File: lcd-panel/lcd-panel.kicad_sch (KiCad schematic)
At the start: 30 parts, among them J1 USB wire, J2 LCD FPC connector, J3 Fan Socket, Q1 AO3400A, U1 FT232HL-REEL, U2 93LC56BT-I/OT, U3 USBLC6-2SC6, Y1 12 MHz, 20 pF load

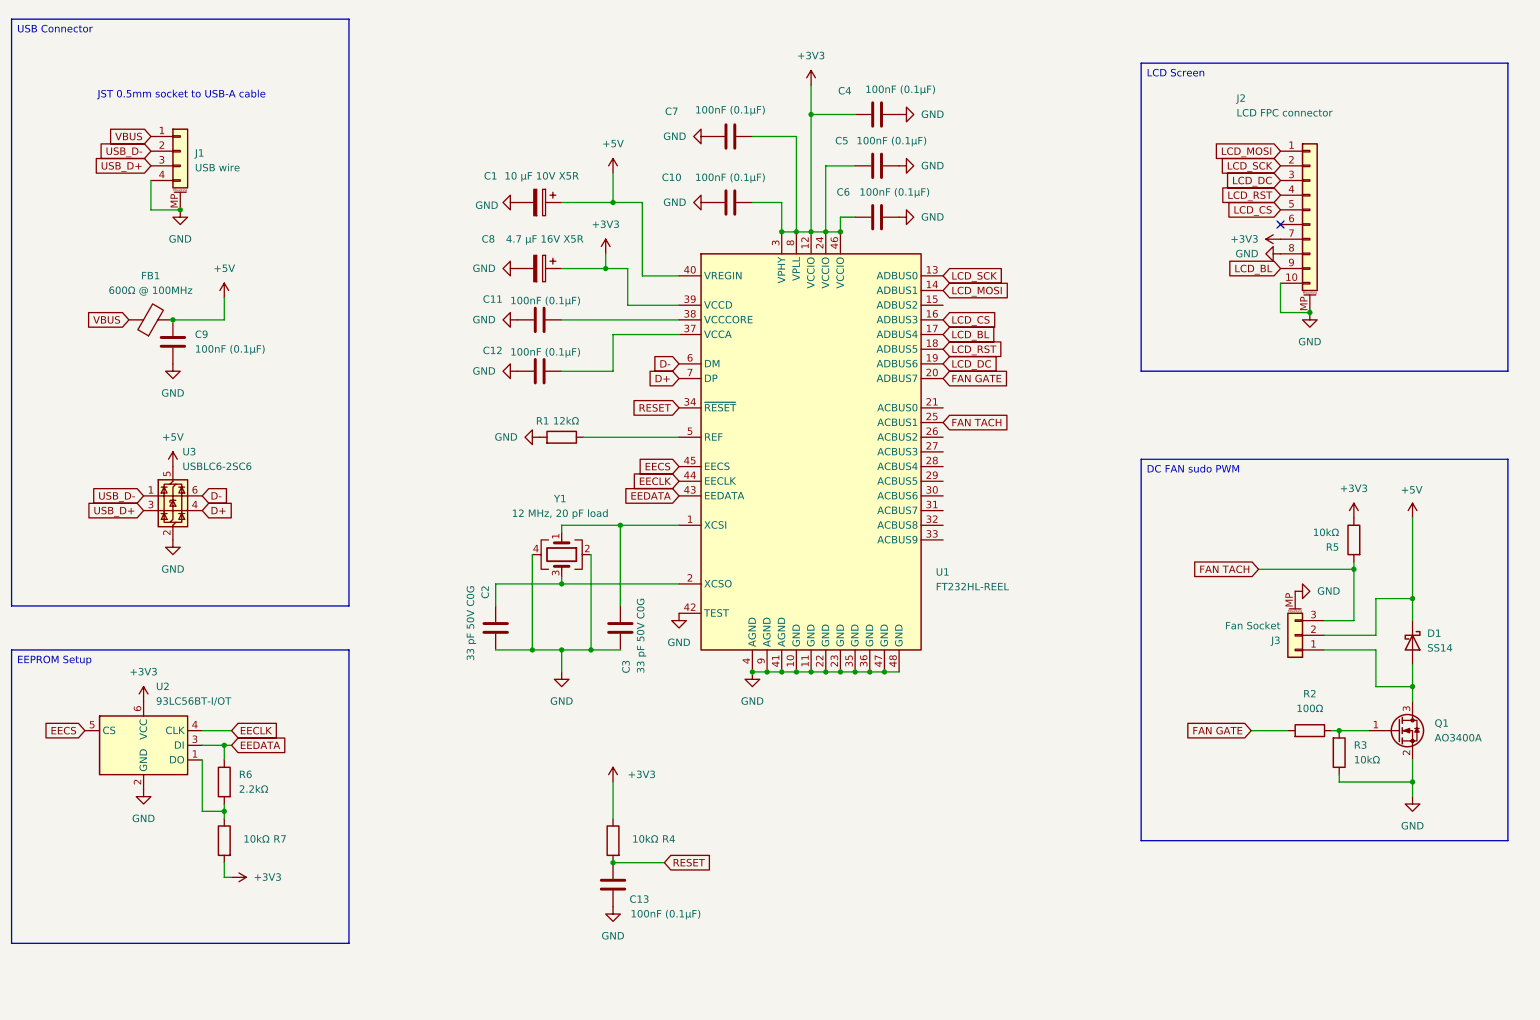
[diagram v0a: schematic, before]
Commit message: Reworking the fan-wiring to add L+C filter to stabilise 3-pin fan voltage from PWM flipping
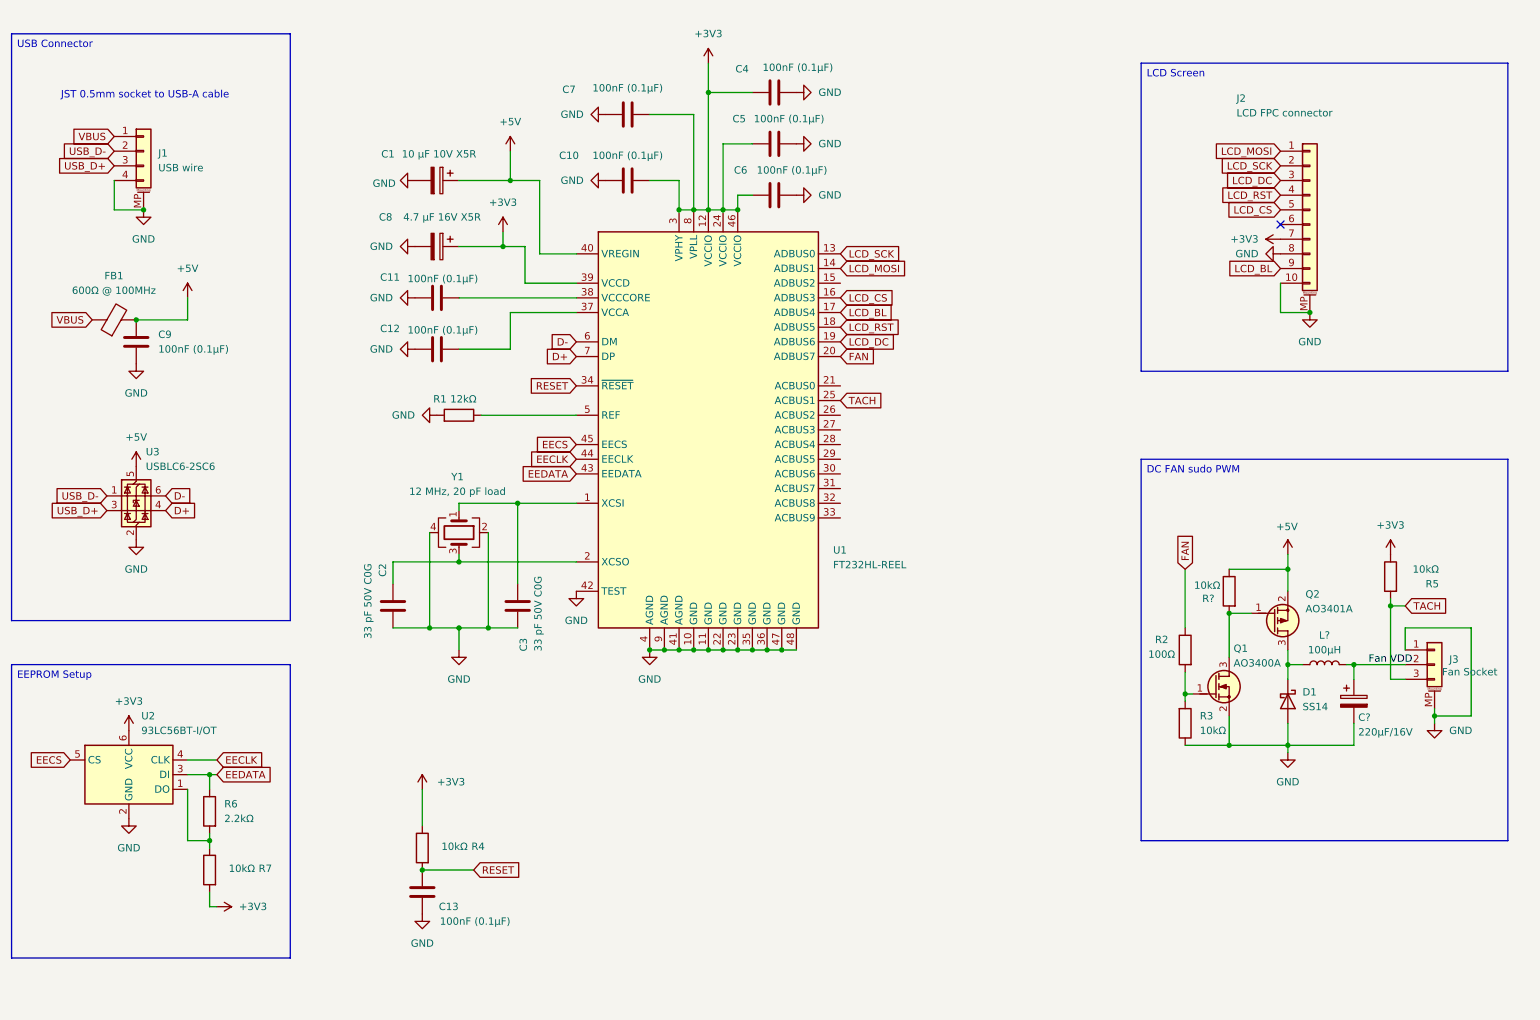
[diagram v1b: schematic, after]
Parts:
- added C?: 220µF/16V, PCM_Capacitor_SMD_AKL:CP_Elec_6.3x7.7, symbol PCM_Capacitor_AKL:CP_SMD_D6.3mm_H7.7mm
- added L?: 100µH, Inductor_SMD:L_Sunlord_SWPA8040S, symbol Device:L
- added Q1: AO3400A, PCM_Package_TO_SOT_SMD_AKL:SOT-23, symbol PCM_Transistor_MOSFET_AKL:AO3400A
- added R?: 10kΩ, Resistor_SMD:R_0402_1005Metric, symbol PCM_Resistor_AKL:R_0603
- Q2: renamed from Q1; value AO3400A -> AO3401A; footprint Package_TO_SOT_SMD:SOT-23 -> PCM_Package_TO_SOT_SMD_AKL:SOT-23; symbol Transistor_FET:AO3400A -> PCM_Transistor_MOSFET_AKL:AO3401A
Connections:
- net +5V: now also Q2.2 (S), R?.2; no longer D1.1 (K), J3.2 (Pin_2)
- net GND: now also D1.2 (A), J3.1 (Pin_1), C?.2, Q1.2 (S); no longer Q2.2 (S)
- net FAN GATE: no longer names the net of R2.1
- net FAN GATE: now also R3.1, Q1.1 (G); no longer U1.20 (ADBUS7)
- net FAN TACH renamed TACH
- new net: D1.1 (K), L?.1, Q2.3 (D)
- new net: Q1.3 (D), Q2.1 (G), R?.1
- new net FAN: R2.2, U1.20 (ADBUS7)
- new net Fan VDD: C?.1, J3.2 (Pin_2), L?.2
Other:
- moved on the sheet: C1, C10, C11, C12, C13, C2, C3, C4, C5, C6, C7, C8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

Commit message: Adding better components to the reworked PWM schematics
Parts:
- C14: renamed from C?; value 220µF/16V -> 22µF 25V X5R; footprint PCM_Capacitor_SMD_AKL:CP_Elec_6.3x7.7 -> PCM_Capacitor_SMD_AKL:C_1206_3216Metric; symbol PCM_Capacitor_AKL:CP_SMD_D6.3mm_H7.7mm -> PCM_Capacitor_AKL:C_1206; LCSC (none) -> C12891
- L1: renamed from L?; footprint Inductor_SMD:L_Sunlord_SWPA8040S -> Inductor_SMD:L_Sunlord_SWPA4018S; LCSC (none) -> C83445
- Q1: LCSC (none) -> C20917
- Q2: LCSC C20917 -> C15127
- R8: renamed from R?; value 10kΩ -> 1kΩ; LCSC C25744 -> C11702
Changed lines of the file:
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@@
 		(on_board yes)
 		(dnp no)
-		(property "Reference" "R?"
+		(property "Reference" "R8"
 			(at 226.06 118.1101 0)
 			(effects
@@
 			)
 		)
-		(property "Value" "10kΩ"
+		(property "Value" "1kΩ"
 			(at 227.076 115.824 0)
 			(effects
@@
 			)
 		)
-		(property "LCSC" "C25744"
+		(property "LCSC" "C11702"
 			(at 228.6 116.84 90)
 			(effects
@@
 			(project "lcd-panel"
 				(path "/79e25751-9ad0-48d5-beb3-fa2c39535c34"
-					(reference "R?")
+					(reference "R8")
 					(unit 1)
 				)
@@
 		)
 		(property "Description" "SOT-23 N-MOSFET enchancement mode transistor, 30V, 5.7A, 1.4W, Alternate KiCAD Library"
+			(at 226.06 133.35 0)
+			(effects
+				(font
+					(size 1.27 1.27)
+				)
+				(hide yes)
+			)
+		)
+		(property "LCSC" "C20917"
 			(at 226.06 133.35 0)
 			(effects
@@
 		(dnp no)
 		(fields_autoplaced yes)
-		(property "Reference" "L?"
+		(property "Reference" "L1"
 			(at 245.11 124.46 90)
 			(effects
@@
 			)
 		)
-		(property "Footprint" "Inductor_SMD:L_Sunlord_SWPA8040S"
+		(property "Footprint" "Inductor_SMD:L_Sunlord_SWPA4018S"
 			(at 245.11 129.54 0)
 			(effects
@@
 			)
 		)
+		(property "LCSC" "C83445"
+			(at 245.11 129.54 90)
+			(effects
+				(font
+					(size 1.27 1.27)
+				)
+				(hide yes)
+			)
+		)
 		(pin "1"
 		)
@@
 			(project ""
 				(path "/79e25751-9ad0-48d5-beb3-fa2c39535c34"
-					(reference "L?")
+					(reference "L1")
 					(unit 1)
 				)
@@
 			)
 		)
-		(property "LCSC" "C20917"
+		(property "LCSC" "C15127"
 			(at 236.22 121.92 0)
 			(effects
@@
 	)
 	(symbol
-		(lib_id "PCM_Capacitor_AKL:CP_SMD_D6.3mm_H7.7mm")
+		(lib_id "PCM_Capacitor_AKL:C_1206")
 		(at 250.19 135.89 0)
 		(unit 1)
@@
 		(on_board yes)
 		(dnp no)
-		(property "Reference" "C?"
-			(at 250.952 138.684 0)
+		(fields_autoplaced yes)
+		(property "Reference" "C14"
+			(at 254 134.6199 0)
 			(effects
 				(font
@@
 			)
 		)
-		(property "Value" "220µF/16V"
-			(at 250.952 141.224 0)
+		(property "Value" "22µF 25V X5R"
+			(at 254 137.1599 0)
 			(effects
 				(font
@@
 			)
 		)
-		(property "Footprint" "PCM_Capacitor_SMD_AKL:CP_Elec_6.3x7.7"
-			(at 250.19 146.05 0)
+		(property "Footprint" "PCM_Capacitor_SMD_AKL:C_1206_3216Metric"
+			(at 251.1552 139.7 0)
 			(effects
 				(font
@@
 			)
 		)
-		(property "Description" "SMD Electrolytic Capacitor, 6.3mm Diameter, 7.7mm Height, European Symbol, Alternate KiCad Library"
+		(property "Description" "SMD 1206 MLCC capacitor, Alternate KiCad Library"
 			(at 250.19 135.89 0)
 			(effects
@@
 			)
 		)
+		(property "LCSC" "C12891"
+			(at 250.19 135.89 0)
+			(effects
+				(font
+					(size 1.27 1.27)
+				)
+				(hide yes)
+			)
+		)
 		(pin "2"
 		)
@@
 			(project ""
 				(path "/79e25751-9ad0-48d5-beb3-fa2c39535c34"
-					(reference "C?")
-					(unit 1)
-				)
+					(reference "C14")
+					(unit 1)
+				)

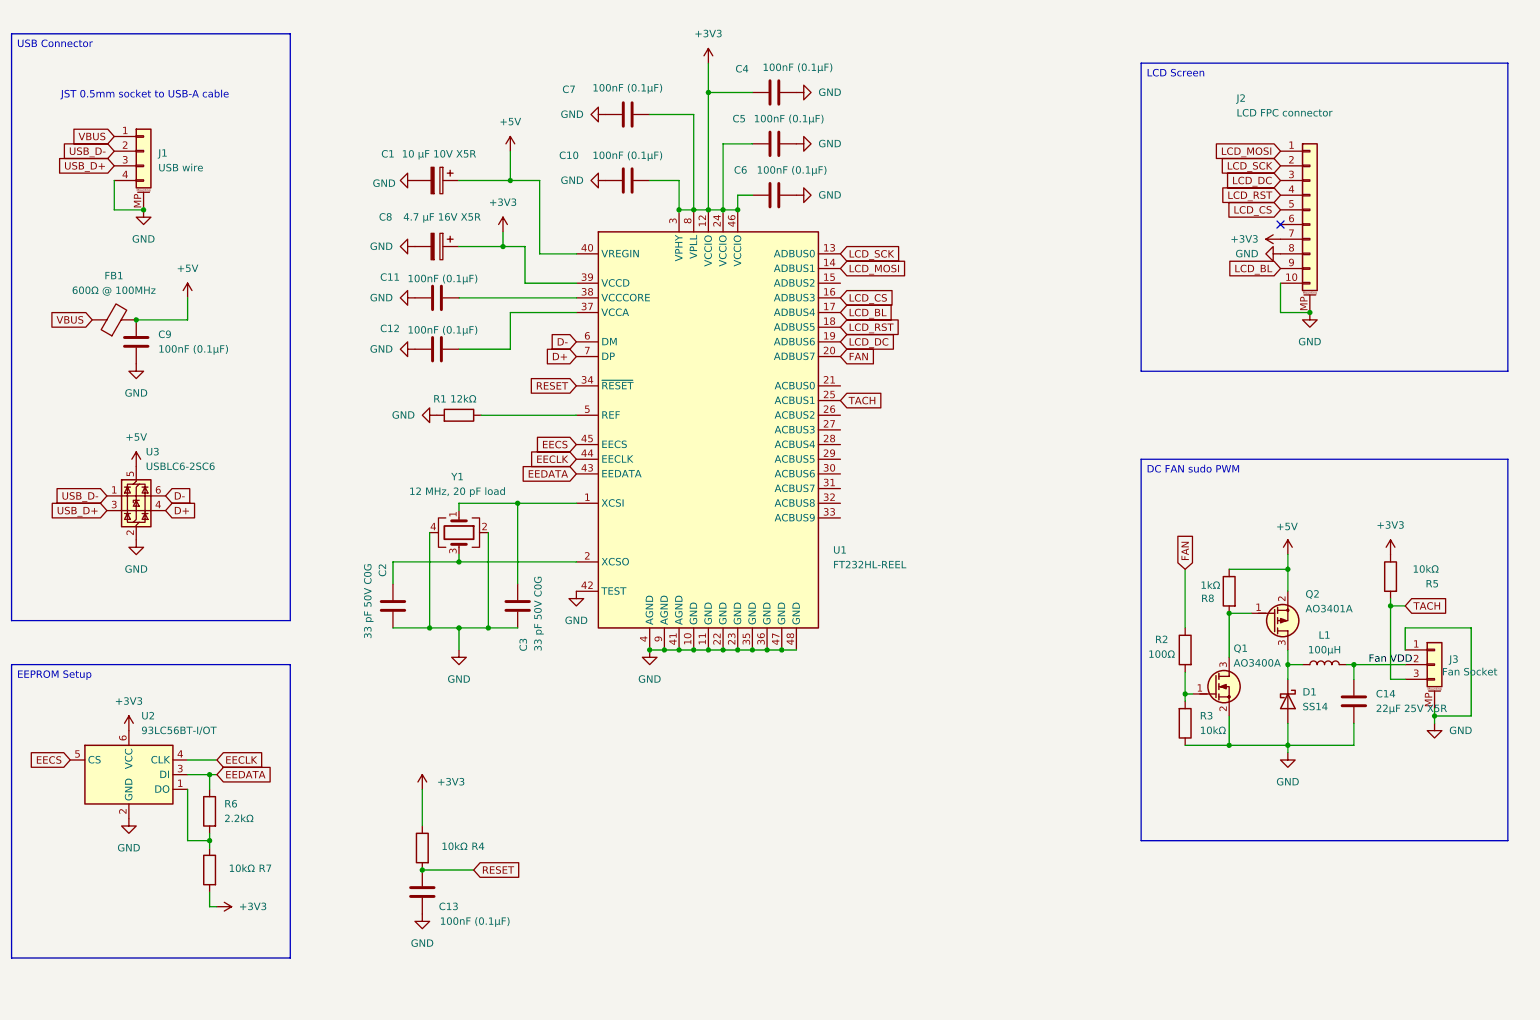
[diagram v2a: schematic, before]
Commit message: Reworking the LCD power supply to control the backlight and give it more juice
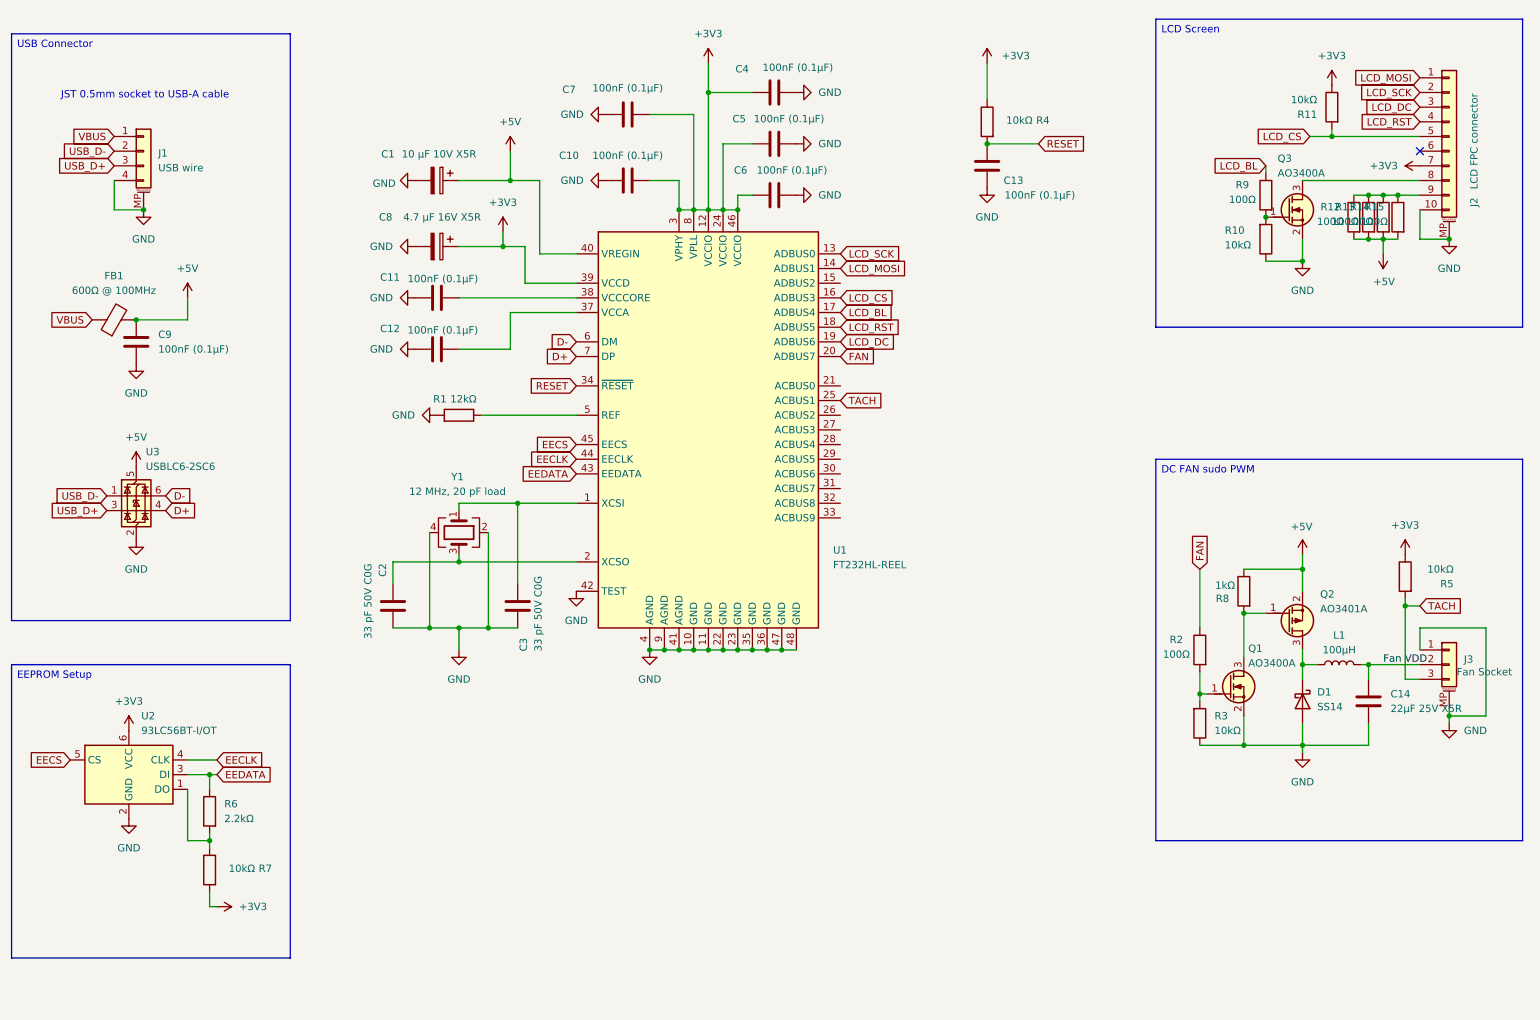
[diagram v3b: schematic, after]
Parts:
- added Q3: AO3400A, PCM_Package_TO_SOT_SMD_AKL:SOT-23, symbol PCM_Transistor_MOSFET_AKL:AO3400A
- added R10, R11: 10kΩ, Resistor_SMD:R_0402_1005Metric, symbol PCM_Resistor_AKL:R_0603
- added R12, R13, R14, R15, R9: 100Ω, Resistor_SMD:R_0603_1608Metric, symbol PCM_Resistor_AKL:R_0603
- R2: footprint Resistor_SMD:R_0402_1005Metric -> Resistor_SMD:R_0603_1608Metric; LCSC C25076 -> C22775
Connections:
- net +3V3: now also R11.2
- net +5V: now also R12.1, R13.1, R14.1, R15.1
- net GND: now also Q3.2 (S), R10.2; no longer J2.8 (Pin_8)
- net LCD_BL: now also R9.2; no longer J2.9 (Pin_9)
- net LCD_CS: now also R11.1
- new net: J2.9 (Pin_9), R12.2, R13.2, R14.2, R15.2
- new net: Q3.1 (G), R10.1, R9.1
- new net: J2.8 (Pin_8), Q3.3 (D)
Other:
- moved on the sheet: C13, C14, D1, J2, J3, L1, Q1, Q2, R2, R3, R4, R5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

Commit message: Reworking the rest of the schematics
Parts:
- added Q4: AO3400A, PCM_Package_TO_SOT_SMD_AKL:SOT-23, symbol PCM_Transistor_MOSFET_AKL:AO3400A
- added Q5: 2N7002, PCM_Package_TO_SOT_SMD_AKL:SOT-23, symbol PCM_Transistor_MOSFET_AKL:2N7002
- added R16, R17, R19: 10kΩ, Resistor_SMD:R_0402_1005Metric, symbol PCM_Resistor_AKL:R_0603
- added R18, R20: 1kΩ, Resistor_SMD:R_0402_1005Metric, symbol PCM_Resistor_AKL:R_0603
- added U4: ATtiny414-SS, Package_SO:SOIC-14_3.9x8.7mm_P1.27mm, symbol MCU_Microchip_ATtiny:ATtiny414-SS
- L1: value 100µH -> 47µH
- R12, R13, R14, R15: value 100Ω -> 120Ω; LCSC C22775 -> C22787
- R2, R9: footprint Resistor_SMD:R_0603_1608Metric -> Resistor_SMD:R_0402_1005Metric; LCSC C22775 -> C25076
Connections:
- net +3V3: now also R16.2, R17.2, R19.1, U4.1 (VCC)
- net FAN: now also U4.9 (PB0); no longer U1.20 (ADBUS7)
- net GND: now also Q4.2 (S), U4.14 (GND)
- net LCD_BL: now also U4.3 (PA5); no longer U1.17 (ADBUS4)
- net TACH: now also U4.8 (PB1); no longer U1.25 (ACBUS1)
- net MISO/DI: now reaches U1.15 (ADBUS2)
- net MISO/DI: now also U4.12 (PA2)
- net /SS TINY: now reaches U1.21 (ACBUS0)
- net /SS TINY: now also U4.2 (PA4)
- net LCD_MOSI renamed MOSI
- net MOSI: now also R20.2, U4.11 (PA1)
- net LCD_SCK renamed SCK
- net SCK: now also R18.2, U4.13 (PA3)
- new net: Q5.3 (D), R18.1, R20.1
- new net: Q4.3 (D), Q5.1 (G), R17.1
- new net SEL/DTR#: Q4.1 (G), R16.1, U1.17 (ADBUS4)
- new net UPDI: Q5.2 (S), R19.2, U4.10 (~{RESET}/PA0)
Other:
- moved on the sheet: C1, C10, C11, C12, C13, C2, C3, C4, C5, C6, C7, C8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
